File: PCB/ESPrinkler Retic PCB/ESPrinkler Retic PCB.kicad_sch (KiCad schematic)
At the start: 17 parts, among them J1 Conn_01x02, J2 Conn_01x02, U1 MOC3063S, U2 LM2596S-5

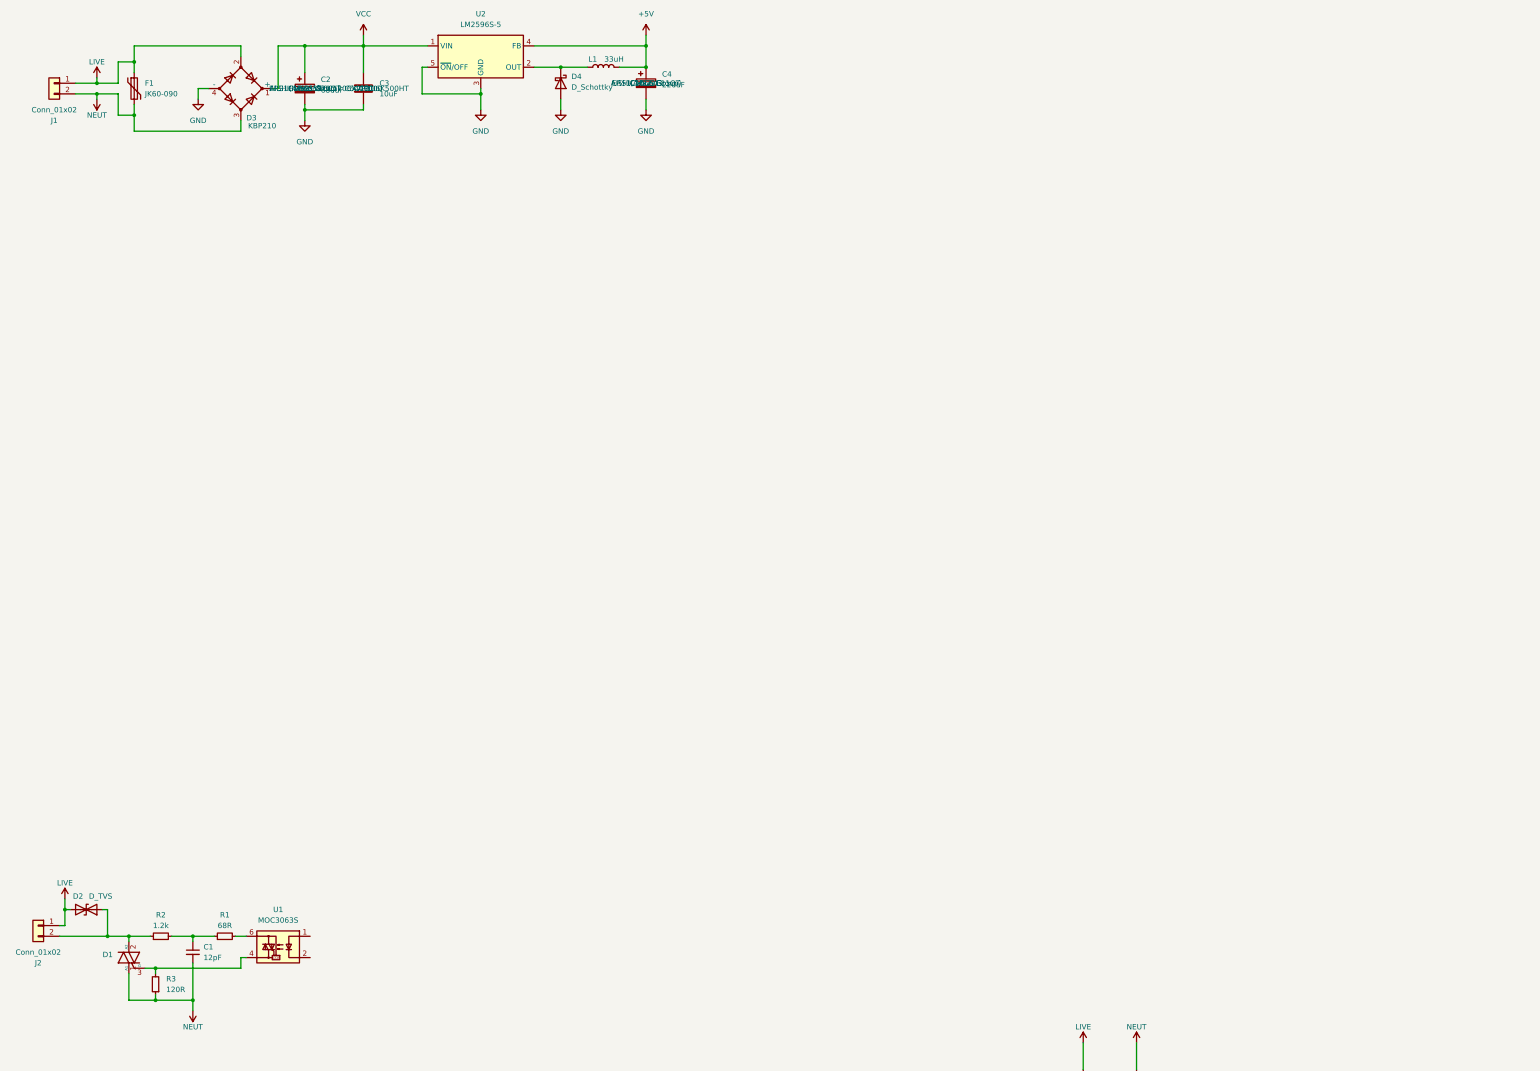
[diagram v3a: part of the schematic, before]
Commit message: Remove part choices due to schematic setup issue, will redo this at some point.
Add headers for ESP32
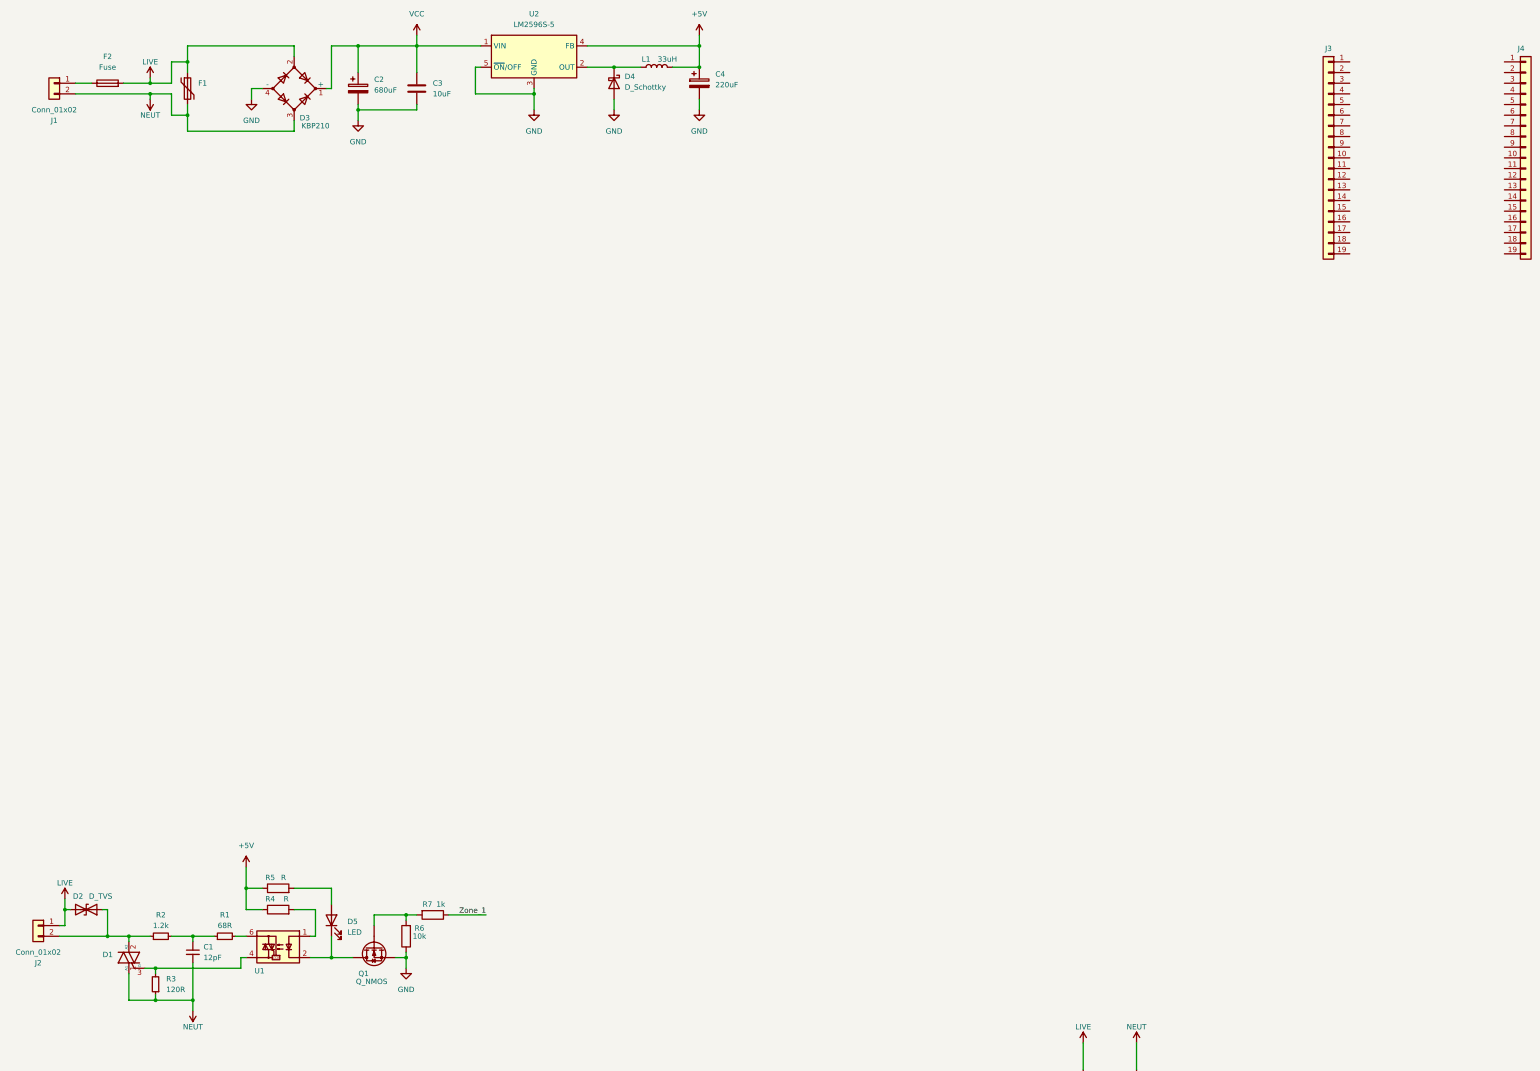
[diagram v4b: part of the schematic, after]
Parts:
- added D5: LED, symbol Device:LED
- added F2: Fuse, symbol Device:Fuse
- added J3, J4: Conn_01x19, symbol Connector_Generic:Conn_01x19
- added Q1: Q_NMOS, symbol Device:Q_NMOS
- added R4, R5: R, symbol Device:R
- added R6: 10k, symbol Device:R
- added R7: 1k, symbol Device:R
- C2: footprint Capacitor_THT:CP_Radial_D12.5mm_P5.00mm -> (none); LCSC Part Number C106668 -> (none); Manufacturer AISHI(Aihua Group) -> (none); Manufacturer Part Number ERS1HM681W20OT -> (none)
- C3: footprint Capacitor_SMD:C_1206_3216Metric -> (none); LCSC Part Number C5449000 -> (none); Manufacturer CCTC -> (none); Manufacturer Part Number TCC1206X7R106K500HT -> (none)
- C4: footprint Capacitor_THT:CP_Radial_D6.3mm_P2.50mm -> (none); LCSC Part Number C106643 -> (none); Manufacturer AISHI(Aihua Group) -> (none); Manufacturer Part Number ERS1CM221E11OT -> (none)
- D3: footprint Diode_THT:Diode_Bridge_Vishay_KBPM -> (none); LCSC Part Number C3081 -> (none); Manufacturer MDD(Microdiode Semiconductor) -> (none); Manufacturer Part Number KBP210 -> (none)
- F1: value JK60-090 -> ~; footprint Fuse:Fuse_Bourns_MF-RHT500 -> (none); LCSC Part Number C369087 -> (none); Manufacturer Jinrui Electronic Materials Co. -> (none); Manufacturer Part Number JK60-090 -> (none)
- U1: value MOC3063S -> ~; footprint Package_DIP:SMDIP-6_W9.53mm -> (none); LCSC Part Number C77950 -> (none); Manufacturer Lite-On -> (none); Manufacturer Part Number MOC3063S-TA1 -> (none)
- U2: LCSC Part Number C347421 -> (none); Manufacturer UMW(Youtai Semiconductor Co., Ltd.) -> (none); Manufacturer Part Number LM2596S-5.0(UMW) -> (none)
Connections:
- net +5V: now also R4.1, R5.1
- net GND: now also Q1.S, R6.1
- net LIVE: now also F2.2; no longer J1.1 (Pin_1)
- net at U1.1: now also R4.2
- net at U1.2: now also D5.1 (K), Q1.D
- new net: F2.1, J1.1 (Pin_1)
- new net: Q1.G, R6.2, R7.2
- new net: D5.2 (A), R5.2
- new net Zone_1: R7.1
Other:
- moved on the sheet: C2, C3, C4, D3, D4, F1, L1, U2

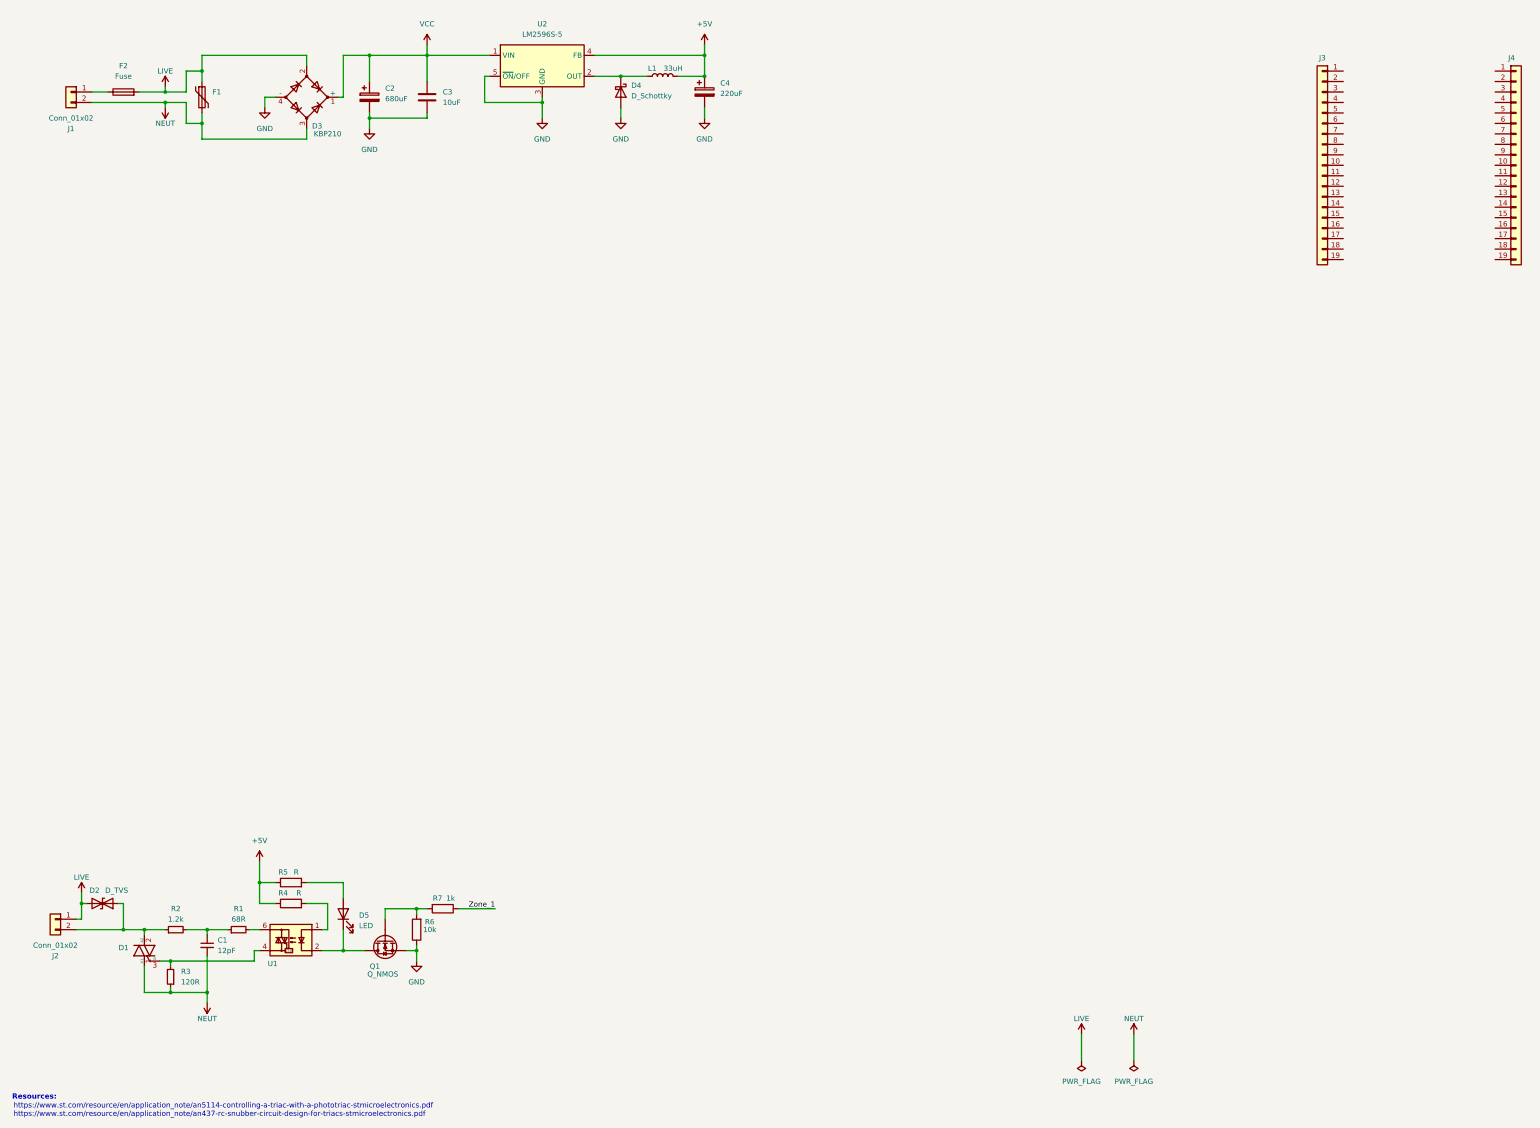
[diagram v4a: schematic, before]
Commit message: Added code to control a Wifi status LED and a general status LED.
Added above onto schematic, start working on ESP32 dev kit pinout
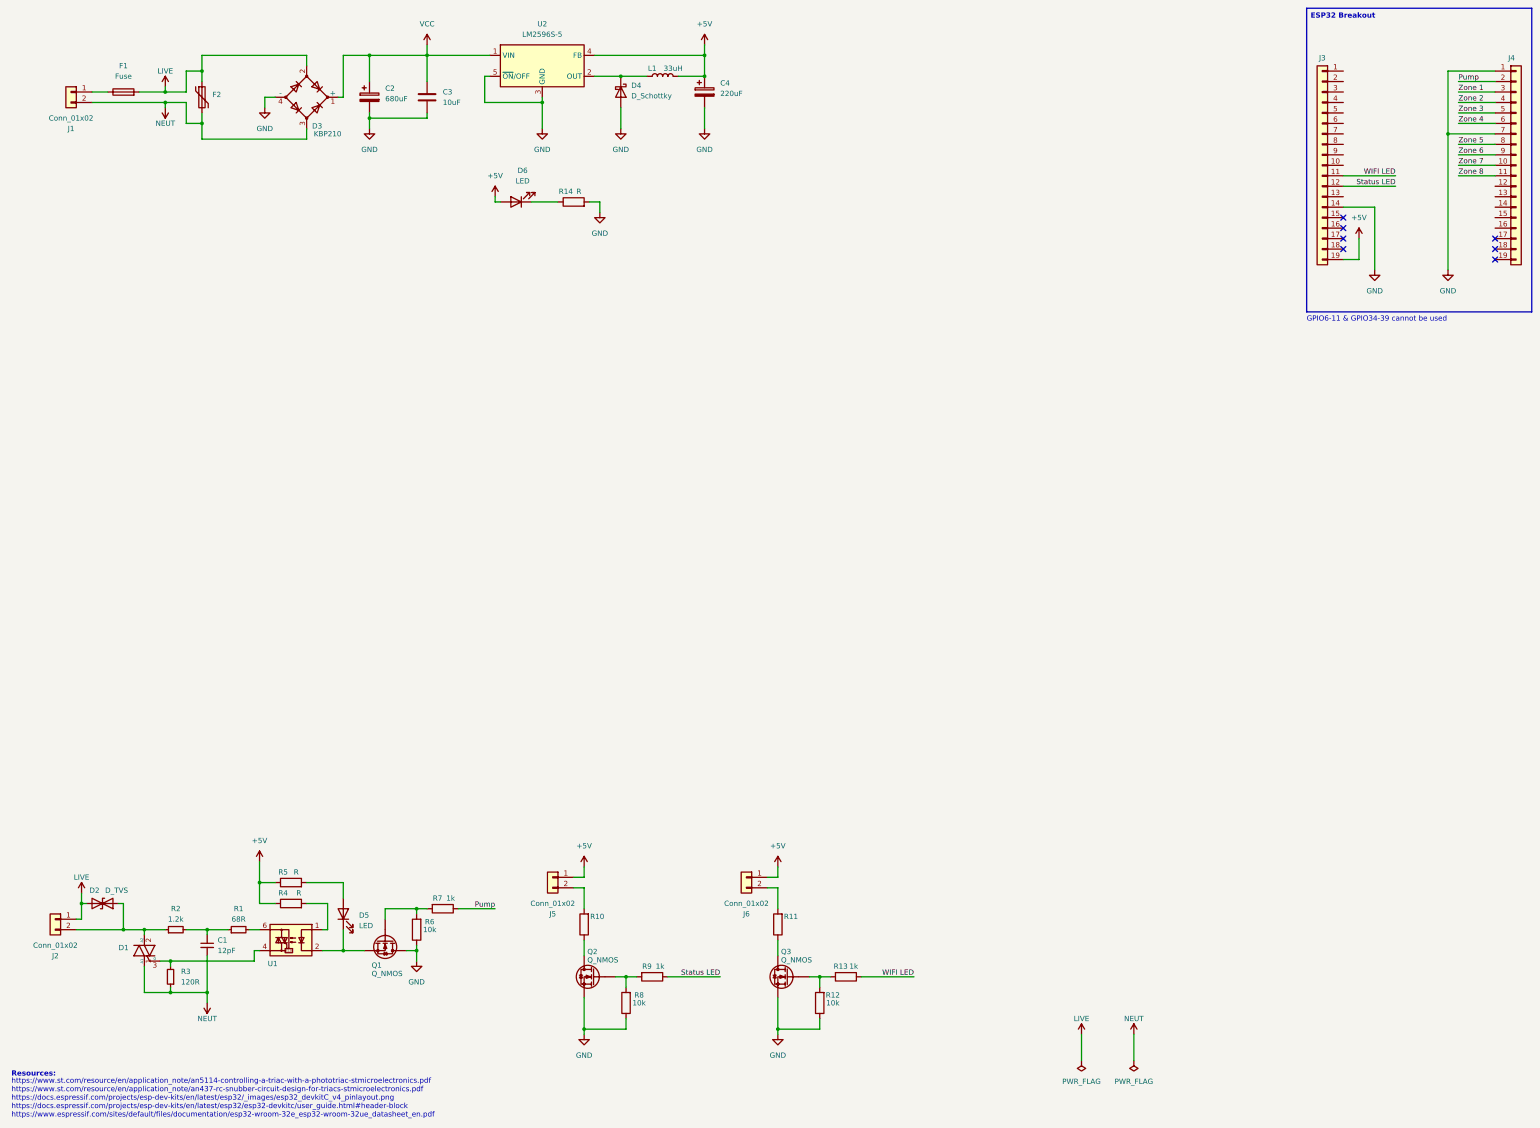
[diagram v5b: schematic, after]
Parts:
- added D6: LED, symbol Device:LED
- added J5, J6: Conn_01x02, symbol Connector_Generic:Conn_01x02
- added Q2, Q3: Q_NMOS, symbol Device:Q_NMOS
- added R10, R11: ~, symbol Device:R
- added R12, R8: 10k, symbol Device:R
- added R13, R9: 1k, symbol Device:R
- added R14: R, symbol Device:R
- renumbered F2 to F1, F1 to F2
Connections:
- net Zone_1 is gone; now on net Pump: R7.1
- net +5V: now also J3.19 (Pin_19), D6.2 (A), J5.1 (Pin_1), J6.1 (Pin_1)
- net GND: now also J3.14 (Pin_14), J4.1 (Pin_1), J4.7 (Pin_7), Q1.D, Q2.S, Q3.S, R12.1, R14.2, R8.1; no longer Q1.S
- net at D5.1 (K), U1.2: now also Q1.S; no longer Q1.D
- net Zone 7: now reaches J4.10 (Pin_10)
- net Zone 8: now reaches J4.11 (Pin_11)
- net Pump: now reaches J4.2 (Pin_2)
- net Zone 1: now reaches J4.3 (Pin_3)
- net Zone 2: now reaches J4.4 (Pin_4)
- net Zone 3: now reaches J4.5 (Pin_5)
- net Zone 4: now reaches J4.6 (Pin_6)
- net Zone 5: now reaches J4.8 (Pin_8)
- net Zone 6: now reaches J4.9 (Pin_9)
- net WIFI LED: now reaches J3.11 (Pin_11)
- net WIFI LED: now also R13.1
- net Status LED: now reaches J3.12 (Pin_12)
- net Status LED: now also R9.1
- new net: D6.1 (K), R14.1
- new net: Q2.G, R8.2, R9.2
- new net: Q3.G, R12.2, R13.2
- new net: Q2.D, R10.1
- new net: Q3.D, R11.1
- new net: J5.2 (Pin_2), R10.2
- new net: J6.2 (Pin_2), R11.2
- no-connect marks 0 -> 7
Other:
- note added: "GPIO6-11 & GPIO34-39 cannot be used"
- note added: "https://www.st.com/resource/en/application_note/an5114-controlling-a-triac-with-a-phototriac-stmicroelectronics.pdf https://www.st.com/resource/en/application_note/an437-rc-snubber-circuit-design-for-triacs-stmicroelectronics.pdf https://docs.espressif.com/projects/esp-dev-kits/en/latest/esp32/_images/esp32_devkitC_v4_pinlayout.png https://docs.espressif.com/projects/esp-dev-kits/en/latest/esp32/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"
- note removed: "https://www.st.com/resource/en/application_note/an5114-controlling-a-triac-with-a-phototriac-stmicroelectronics.pdf https://www.st.com/resource/en/application_note/an437-rc-snubber-circuit-design-for-triacs-stmicroelectronics.pdf"
- moved on the sheet: Q1

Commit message: Begin muilti-sheet design to organise schematic better
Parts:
- removed J2: Conn_01x02, symbol Connector_Generic:Conn_01x02
- removed J3, J4: Conn_01x19, symbol Connector_Generic:Conn_01x19
- added J7: Conn_01x10, symbol Connector_Generic:Conn_01x10
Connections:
- net NEUT: now also J7.1 (Pin_1); no longer C1.2, D1.1 (A1), R3.1
- new net: C1.2, D1.1 (A1), J7.2 (Pin_2), R3.1
- no-connect marks 7 -> 0
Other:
- added sheet Control Outputs (Control Outputs.kicad_sch)
- added sheet ESP32 (ESP32.kicad_sch)
- added sheet Power (power.kicad_sch)
- note removed: "GPIO6-11 & GPIO34-39 cannot be used"
- moved on the sheet: C1, C2, C3, C4, D1, D2, D3, D4, D5, D6, F1, F2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

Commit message: Continue migrating PCB project to multi sheet design
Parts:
- removed C1: 12pF, symbol Device:C_Small
- removed C2: 680uF, symbol Device:C_Polarized
- removed C3: 10uF, symbol Device:C
- removed C4: 220uF, symbol Device:C_Polarized
- removed D1: Generic_Triac_A1A2G, symbol Triac_Thyristor:Generic_Triac_A1A2G
- removed D2: D_TVS, symbol Device:D_TVS
- removed D3: KBP210, symbol Device:D_Bridge_+AA-
- removed D4: D_Schottky, symbol Device:D_Schottky
- removed D5, D6: LED, symbol Device:LED
- removed F1: Fuse, symbol Device:Fuse
- removed F2: ~, symbol Device:Polyfuse
- removed J1, J5, J6: Conn_01x02, symbol Connector_Generic:Conn_01x02
- removed J7: Conn_01x10, symbol Connector_Generic:Conn_01x10
- removed L1: 33uH, symbol Device:L
- removed Q1, Q2, Q3: Q_NMOS, symbol Device:Q_NMOS
- removed R1: 68R, symbol Device:R_Small
- removed R10, R11: ~, symbol Device:R
- removed R12, R6, R8: 10k, symbol Device:R
- removed R13, R7, R9: 1k, symbol Device:R
- removed R14, R4, R5: R, symbol Device:R
- removed R2: 1.2k, symbol Device:R_Small
- removed R3: 120R, symbol Device:R_Small
- removed U1: ~, symbol Relay_SolidState:MOC3063M
- removed U2: LM2596S-5, Package_TO_SOT_SMD:TO-263-5_TabPin3, symbol Regulator_Switching:LM2596S-5
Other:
- removed sheet Control Outputs
- removed sheet ESP32
- removed sheet Power
- added sheet Power & IO (Power IO.kicad_sch)
